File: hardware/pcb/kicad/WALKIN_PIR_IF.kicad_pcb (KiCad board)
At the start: 2 copper layers, 67.1 x 42.9 mm, 22 parts, among them J1 Battery Terminal, J2 XWA11V Terminal, J3 Probe Terminal, Q1 AO3401A, U1 AQY212EH

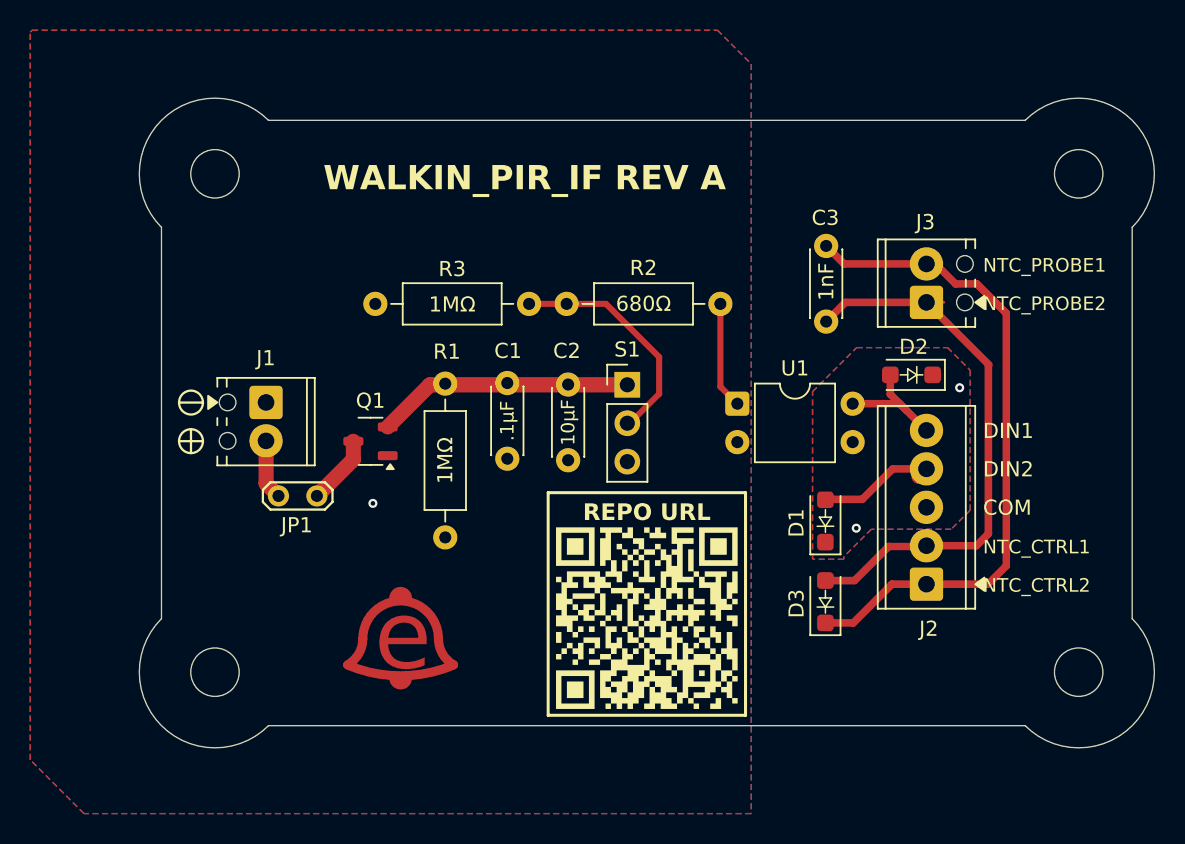
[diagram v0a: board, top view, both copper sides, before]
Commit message: Added npn low side driver for photomos cathode for rev B
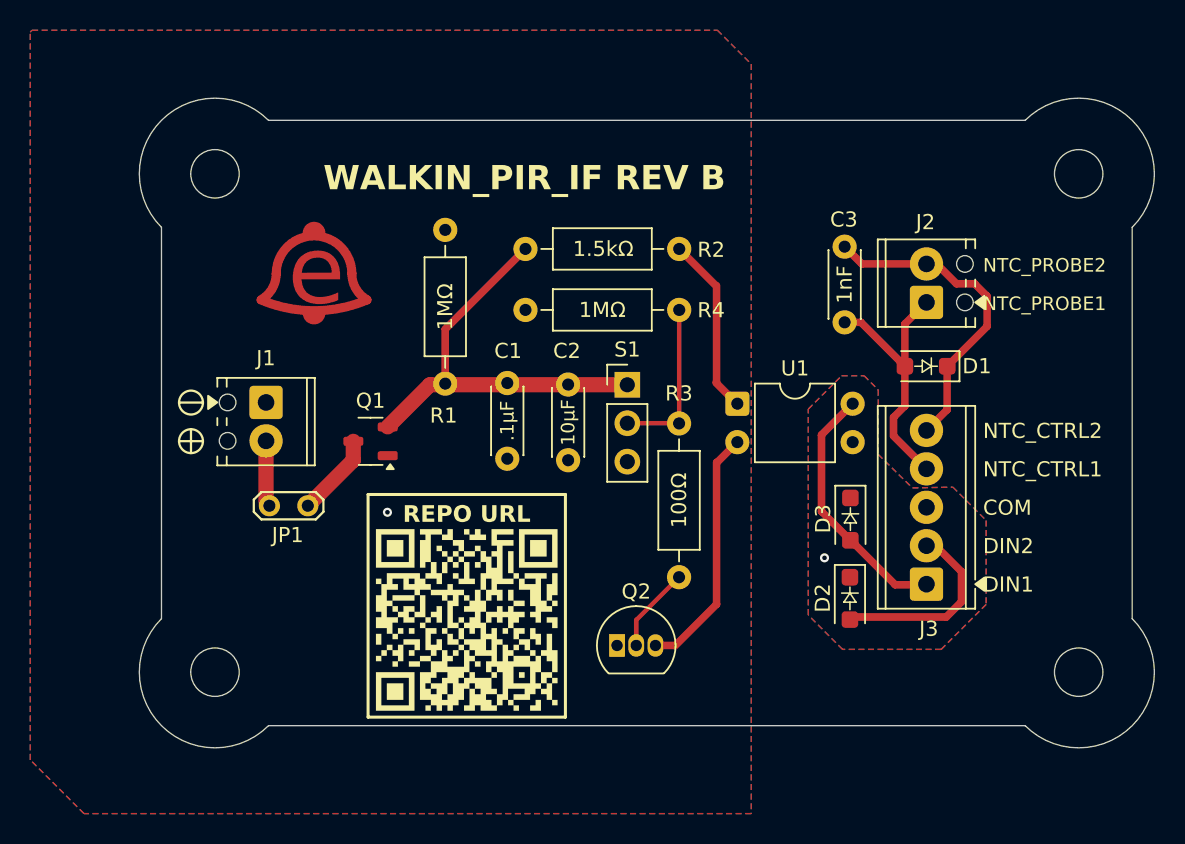
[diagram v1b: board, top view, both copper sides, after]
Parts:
- added Q2: 2N7000, Package_TO_SOT_THT:TO-92_Inline, F.Cu at (153.0, 112.1)
- added R3: 100Ω, Resistor_THT:R_Axial_DIN0207_L6.3mm_D2.5mm_P10.16mm_Horizontal, F.Cu at (157.1, 97.5)
- R2: value 680Ω -> 1.5kΩ
- moved REF** 24.8 mm to (133.1, 87.5)
- moved D2 15.3 mm to (168.4, 109.0), turned to -90 degrees
- moved D1 12.2 mm to (173.4, 93.7), turned to 180 degrees
- moved G*** 11.9 mm to (143.1, 110.4)
- moved R4 9.93 mm to (157.1, 90.0)
- moved D3 5.70 mm to (168.4, 103.8), turned to -90 degrees
- moved R2 4.54 mm to (147.0, 85.9)
- moved C3 1.22 mm to (168.1, 90.8)
- moved JP1 0.88 mm to (130.1, 102.9)
- turned R1 to 90 degrees
- renumbered J3 to J2, J2 to J3, R3 to R4
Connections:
- D1 pad 1: /COM -> /NTC2
- D1 pad 2: /DIN2 -> /NTC1
- D2 pad 2: /DIN1 -> /DIN2
- D3 pad 1: /NTC2 -> /COM
- D3 pad 2: /NTC1 -> /DIN1
- J3 pad 1: /NTC2 -> /DIN1
- J3 pad 2: /NTC1 -> /DIN2
- J3 pad 4: /DIN2 -> /NTC1
- J3 pad 5: /DIN1 -> /NTC2
- R2 pad 1: Net-(S1-VOUT) -> VDD
- R2 pad 2: /PIR_SIG -> /PM_LED_A
- R4 pad 1: Net-(S1-VOUT) -> /PIR_SIG
- S1 pad 2: Net-(S1-VOUT) -> /PIR_SIG
- U1 pad 1: /PIR_SIG -> /PM_LED_A
- U1 pad 2: GND -> /PM_LED_K
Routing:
- net /NTC2: track 43.9 -> 22.3 mm
- net /NTC1: track 37.3 -> 18.5 mm
- net /PM_LED_K: track 0.00 -> 16.5 mm
- net Net-(S1-VOUT): track 15.4 -> 0.00 mm
- net VDD: track 17.0 -> 29.3 mm
- net /PM_LED_A: track 0.00 -> 11.8 mm
- net /DIN1: track 8.36 -> 16.9 mm
- net Net-(Q2-G): track 0.00 -> 5.68 mm
- net /DIN2: track 8.70 -> 12.9 mm
- net /PIR_SIG: track 7.06 -> 10.9 mm
- net Net-(JP1-B): track 4.65 -> 5.55 mm
- net /COM: track 0.88 -> 0.57 mm, vias 2 -> 1
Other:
- board text added: "1.5kΩ"
- board text added: "100Ω"
- board text removed: "680Ω"

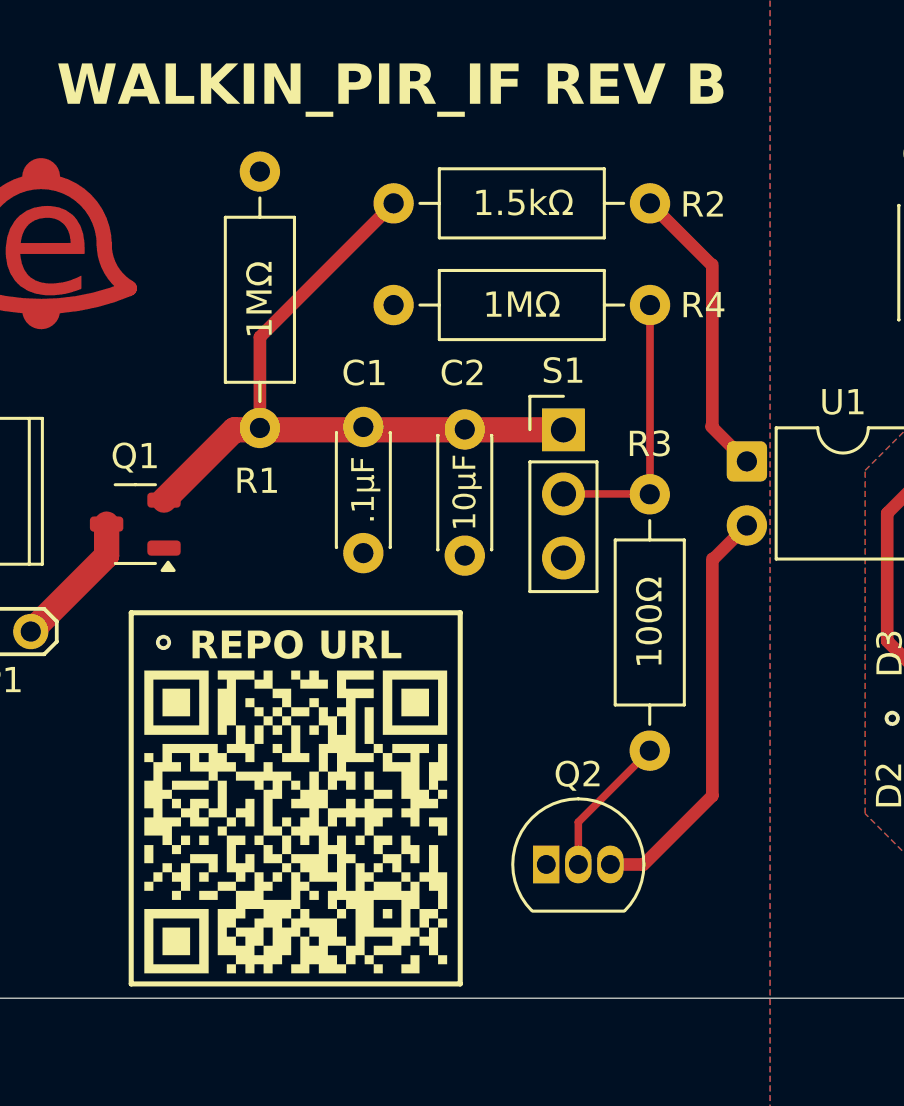
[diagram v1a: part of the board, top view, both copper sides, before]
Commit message: moved pir pulldown r to npn gate and changed value to 100k
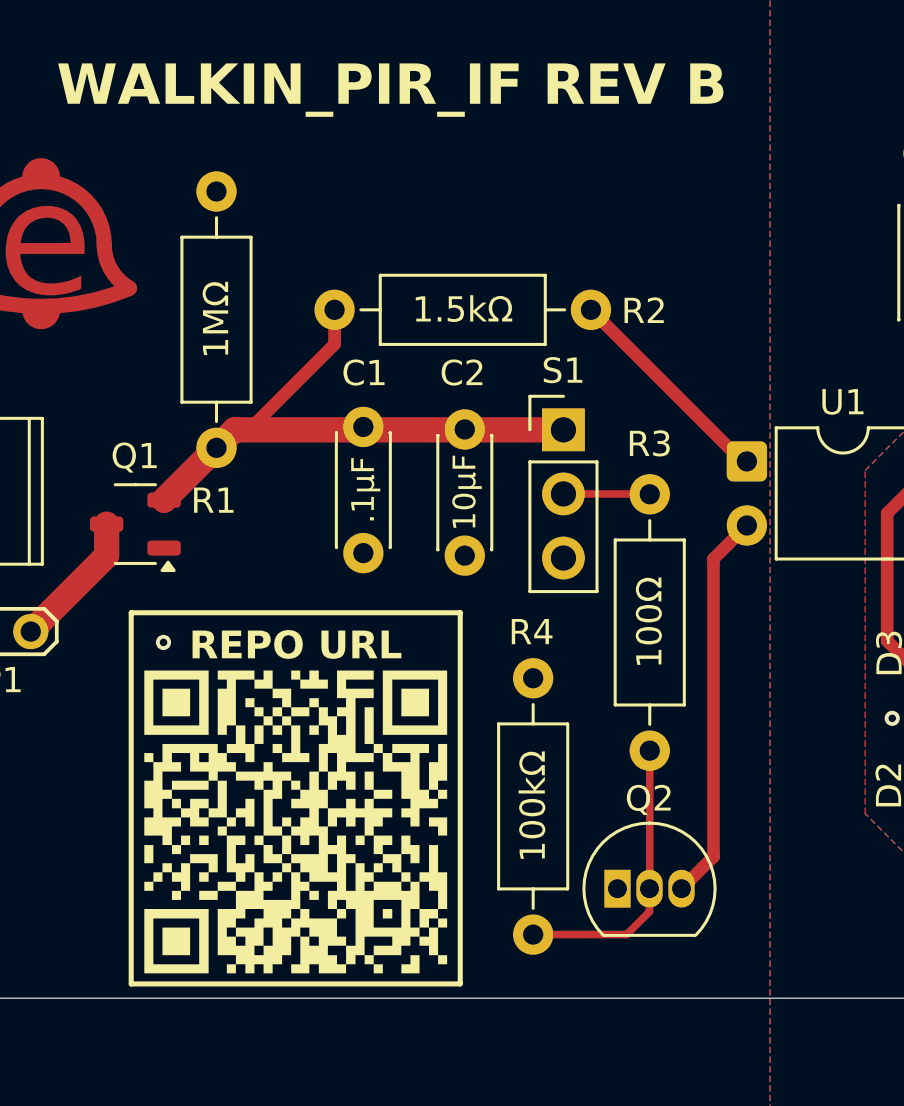
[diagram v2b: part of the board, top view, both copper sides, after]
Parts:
- R4: value 1MΩ -> 100kΩ
- moved R4 25.4 mm to (152.5, 114.9), turned to 90 degrees
- moved R2 4.83 mm to (144.6, 90.1)
- moved Q2 2.98 mm to (155.8, 113.1)
- moved R1 1.89 mm to (139.9, 95.6)
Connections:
- R4 pad 1: /PIR_SIG -> Net-(Q2-G)
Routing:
- net /PIR_SIG: track 10.9 -> 3.46 mm
- net Net-(Q2-G): track 5.68 -> 11.4 mm
- net VDD: track 29.3 -> 23.7 mm
- net /PM_LED_A: track 11.8 -> 8.67 mm
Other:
- board text added: "100kΩ"
